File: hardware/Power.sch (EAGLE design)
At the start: 8 parts, among them IC1 ATmega328P, Q1 16mHz

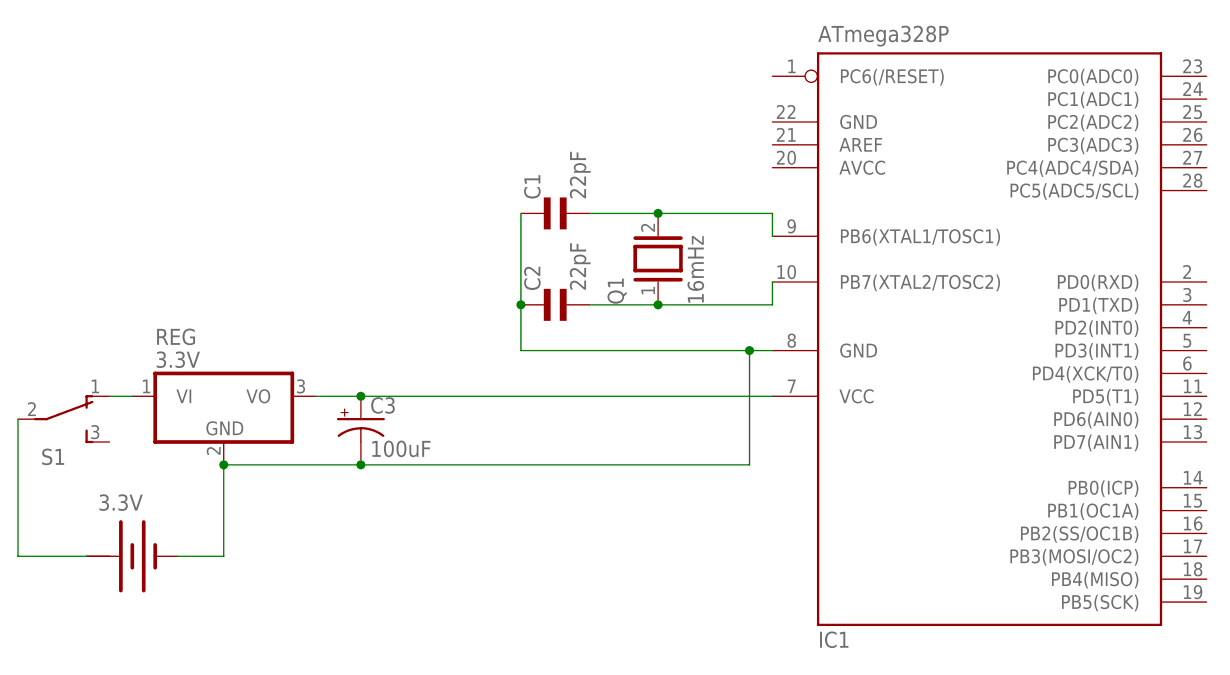
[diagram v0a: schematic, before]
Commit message: Added missing RESET/AVCC connections and eliminated short circuit in off switch
Resized schematics to conform image sizes
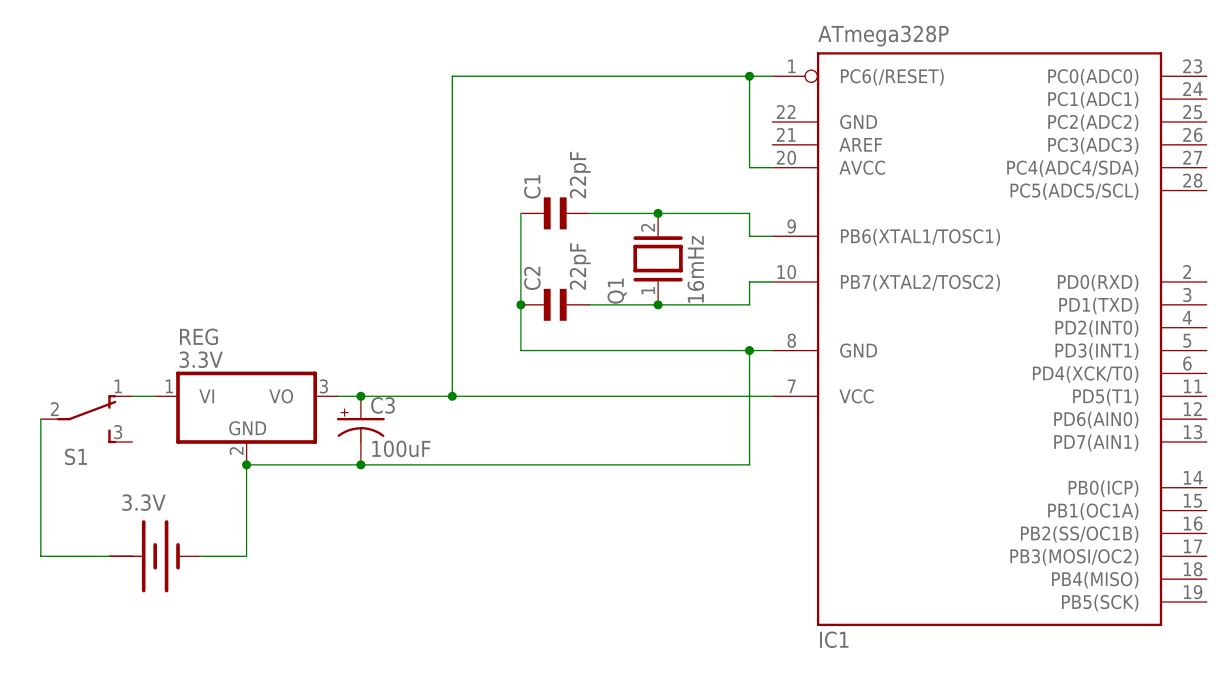
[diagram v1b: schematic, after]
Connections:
- net N$3: now also IC1.AVCC, IC1.PC6(/RESET)
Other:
- moved on the sheet: 3.3V, REG, S1
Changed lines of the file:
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@@
 <instances>
 <instance part="IC1" gate="G$1" x="114.3" y="38.1"/>
-<instance part="REG" gate="A" x="30.48" y="30.48"/>
-<instance part="3.3V" gate="G$1" x="20.32" y="12.7"/>
+<instance part="REG" gate="A" x="33.02" y="30.48"/>
+<instance part="3.3V" gate="G$1" x="22.86" y="12.7"/>
 <instance part="Q1" gate="G$1" x="78.74" y="45.72" rot="R90"/>
 <instance part="C1" gate="G$1" x="66.04" y="50.8" rot="R90"/>
 <instance part="C2" gate="G$1" x="66.04" y="40.64" rot="R90"/>
-<instance part="S1" gate="BEF1" x="12.7" y="27.94" rot="R270"/>
+<instance part="S1" gate="BEF1" x="15.24" y="27.94" rot="R270"/>
 <instance part="C3" gate="G$1" x="45.72" y="27.94"/>
 </instances>
@@
 <pinref part="REG" gate="A" pin="VI"/>
 <pinref part="S1" gate="BEF1" pin="O"/>
-<wire x1="20.32" y1="30.48" x2="17.78" y2="30.48" width="0.1524" layer="91"/>
+<wire x1="22.86" y1="30.48" x2="20.32" y2="30.48" width="0.1524" layer="91"/>
 </segment>
 </net>
@@
 <pinref part="REG" gate="A" pin="GND"/>
 <pinref part="3.3V" gate="G$1" pin="-"/>
-<wire x1="25.4" y1="12.7" x2="30.48" y2="12.7" width="0.1524" layer="91"/>
-<wire x1="30.48" y1="12.7" x2="30.48" y2="22.86" width="0.1524" layer="91"/>
-<junction x="30.48" y="22.86"/>
-<wire x1="30.48" y1="22.86" x2="45.72" y2="22.86" width="0.1524" layer="91"/>
+<wire x1="27.94" y1="12.7" x2="33.02" y2="12.7" width="0.1524" layer="91"/>
+<wire x1="33.02" y1="12.7" x2="33.02" y2="22.86" width="0.1524" layer="91"/>
+<junction x="33.02" y="22.86"/>
+<wire x1="33.02" y1="22.86" x2="45.72" y2="22.86" width="0.1524" layer="91"/>
 <pinref part="IC1" gate="G$1" pin="GND@1"/>
 <wire x1="45.72" y1="22.86" x2="88.9" y2="22.86" width="0.1524" layer="91"/>
@@
 <segment>
 <pinref part="S1" gate="BEF1" pin="P"/>
-<wire x1="7.62" y1="27.94" x2="7.62" y2="12.7" width="0.1524" layer="91"/>
+<wire x1="10.16" y1="27.94" x2="10.16" y2="12.7" width="0.1524" layer="91"/>
 <pinref part="3.3V" gate="G$1" pin="+"/>
-<wire x1="7.62" y1="12.7" x2="15.24" y2="12.7" width="0.1524" layer="91"/>
+<wire x1="10.16" y1="12.7" x2="17.78" y2="12.7" width="0.1524" layer="91"/>
 </segment>
 </net>
@@
 <pinref part="REG" gate="A" pin="VO"/>
 <pinref part="IC1" gate="G$1" pin="VCC@1"/>
-<wire x1="40.64" y1="30.48" x2="45.72" y2="30.48" width="0.1524" layer="91"/>
+<wire x1="43.18" y1="30.48" x2="45.72" y2="30.48" width="0.1524" layer="91"/>
 <pinref part="C3" gate="G$1" pin="+"/>
-<wire x1="45.72" y1="30.48" x2="91.44" y2="30.48" width="0.1524" layer="91"/>
+<wire x1="45.72" y1="30.48" x2="55.88" y2="30.48" width="0.1524" layer="91"/>
 <junction x="45.72" y="30.48"/>
+<wire x1="55.88" y1="30.48" x2="91.44" y2="30.48" width="0.1524" layer="91"/>
+<wire x1="55.88" y1="30.48" x2="55.88" y2="66.04" width="0.1524" layer="91"/>
+<pinref part="IC1" gate="G$1" pin="PC6(/RESET)"/>
+<wire x1="55.88" y1="66.04" x2="88.9" y2="66.04" width="0.1524" layer="91"/>
+<wire x1="88.9" y1="66.04" x2="91.44" y2="66.04" width="0.1524" layer="91"/>
+<wire x1="88.9" y1="66.04" x2="88.9" y2="55.88" width="0.1524" layer="91"/>
+<pinref part="IC1" gate="G$1" pin="AVCC"/>
+<wire x1="88.9" y1="55.88" x2="91.44" y2="55.88" width="0.1524" layer="91"/>
+<junction x="88.9" y="66.04"/>
+<junction x="55.88" y="30.48"/>
 </segment>
 </net>
@@
 <segment>
 <pinref part="Q1" gate="G$1" pin="2"/>
-<wire x1="78.74" y1="50.8" x2="91.44" y2="50.8" width="0.1524" layer="91"/>
+<wire x1="78.74" y1="50.8" x2="88.9" y2="50.8" width="0.1524" layer="91"/>
+<wire x1="91.44" y1="48.26" x2="88.9" y2="48.26" width="0.1524" layer="91"/>
+<wire x1="88.9" y1="48.26" x2="88.9" y2="50.8" width="0.1524" layer="91"/>
 <pinref part="IC1" gate="G$1" pin="PB6(XTAL1/TOSC1)"/>
-<wire x1="91.44" y1="50.8" x2="91.44" y2="48.26" width="0.1524" layer="91"/>
 <pinref part="C1" gate="G$1" pin="2"/>
 <wire x1="71.12" y1="50.8" x2="78.74" y2="50.8" width="0.1524" layer="91"/>
@@
 <segment>
 <pinref part="Q1" gate="G$1" pin="1"/>
-<wire x1="78.74" y1="40.64" x2="91.44" y2="40.64" width="0.1524" layer="91"/>
+<wire x1="78.74" y1="40.64" x2="88.9" y2="40.64" width="0.1524" layer="91"/>
 <pinref part="IC1" gate="G$1" pin="PB7(XTAL2/TOSC2)"/>
-<wire x1="91.44" y1="40.64" x2="91.44" y2="43.18" width="0.1524" layer="91"/>
+<wire x1="88.9" y1="40.64" x2="88.9" y2="43.18" width="0.1524" layer="91"/>
+<wire x1="88.9" y1="43.18" x2="91.44" y2="43.18" width="0.1524" layer="91"/>
 <pinref part="C2" gate="G$1" pin="2"/>
 <wire x1="71.12" y1="40.64" x2="78.74" y2="40.64" width="0.1524" layer="91"/>
